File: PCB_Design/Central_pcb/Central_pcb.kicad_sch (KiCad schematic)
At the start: 1 part, among them U3 nRF52832-QFxx

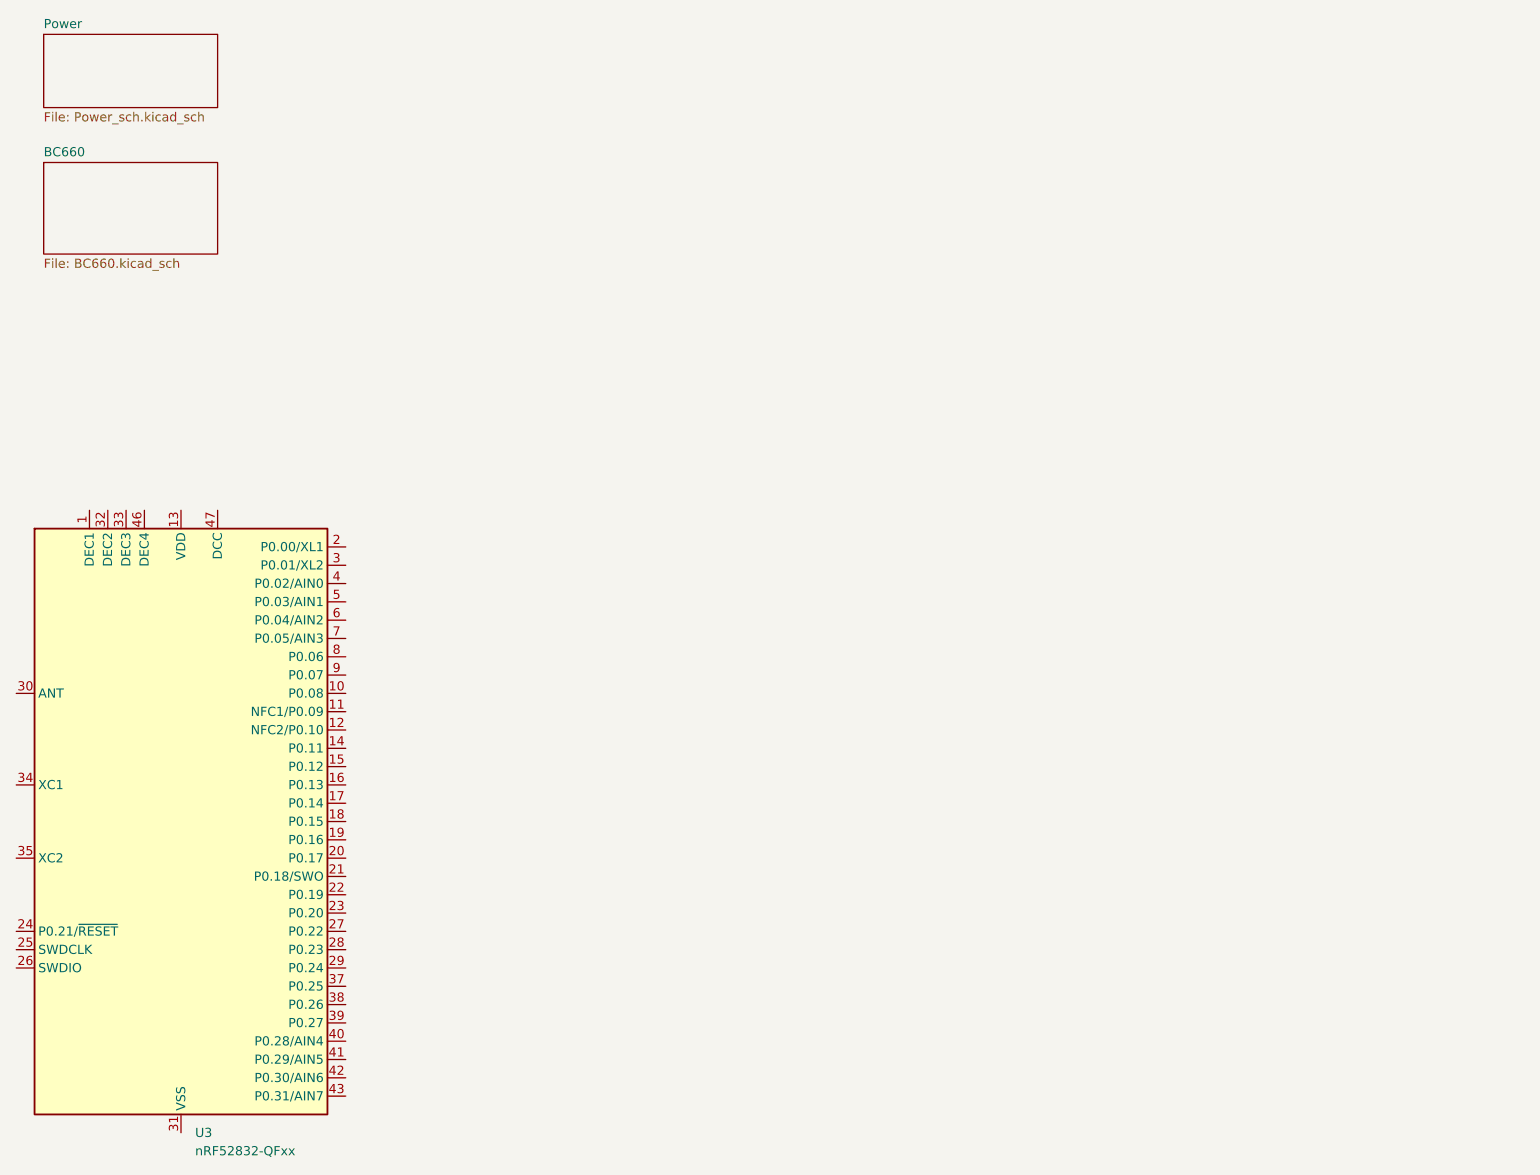
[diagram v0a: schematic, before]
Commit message: Power part added
Power part is finished with power footprints
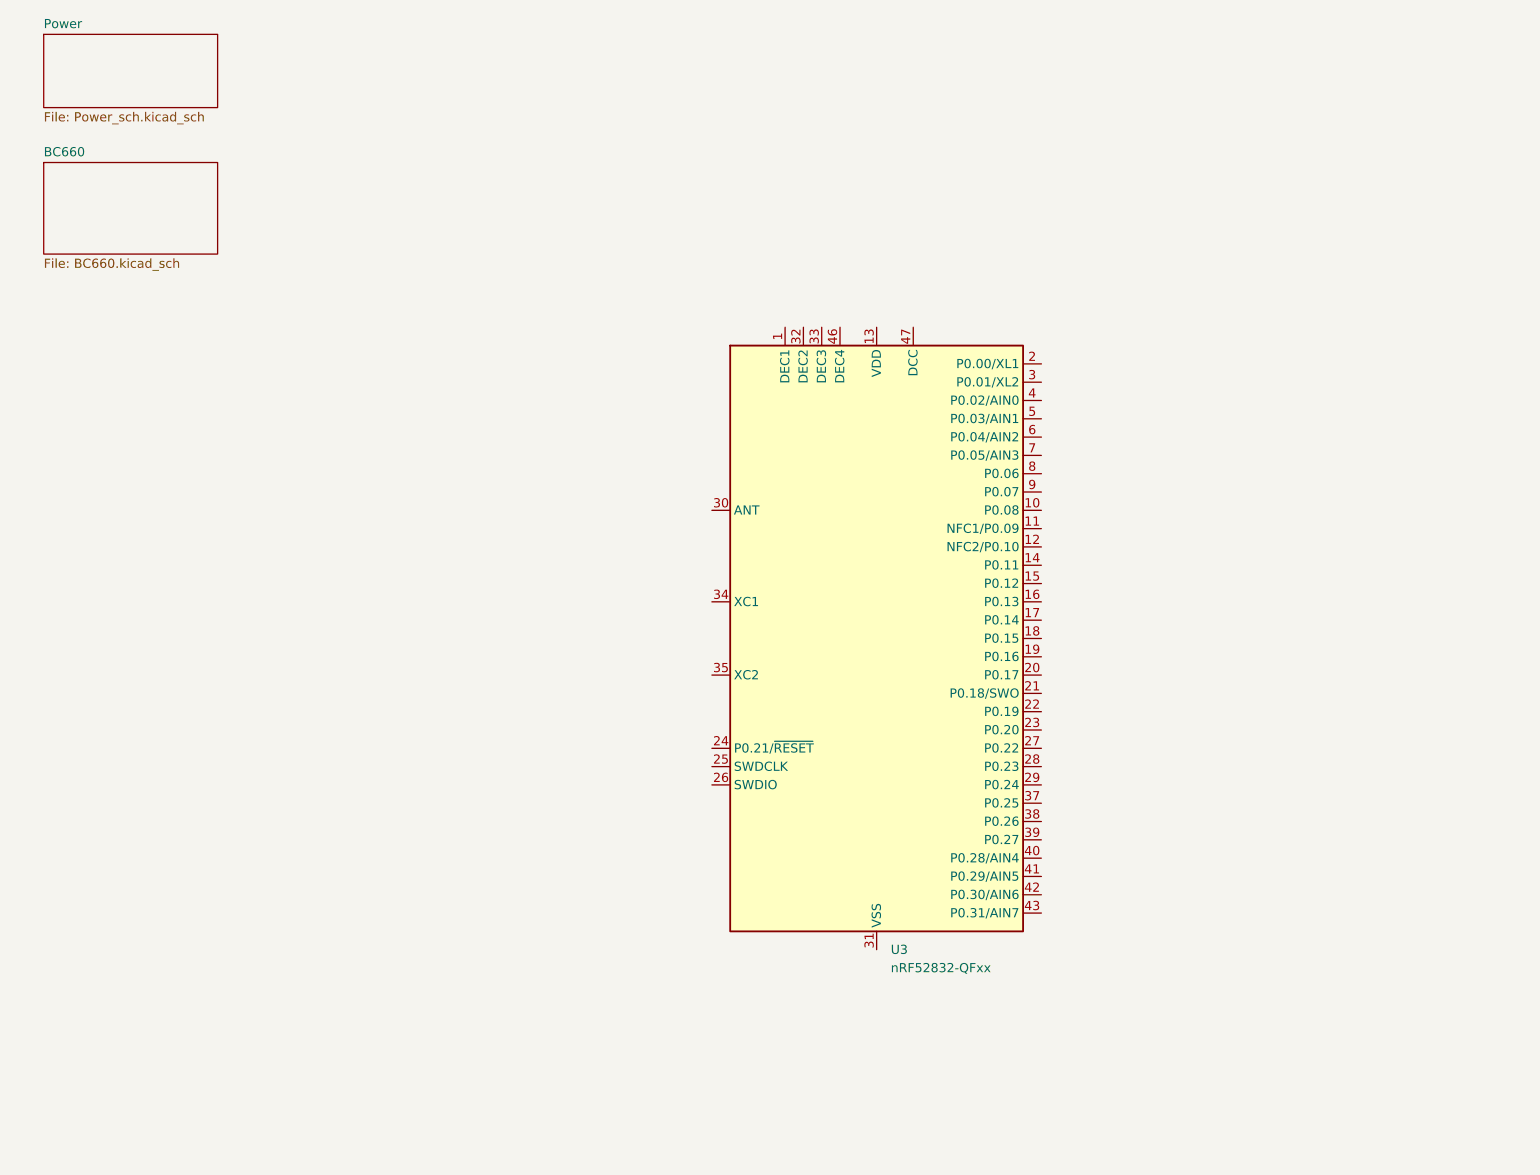
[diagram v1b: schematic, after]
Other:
- moved on the sheet: U3
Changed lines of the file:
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@@
 (kicad_sch (version 20230121) (generator eeschema)
   (paper "A4")
-  (symbol (lib_id "MCU_Nordic:nRF52832-QFxx") (at 45.72 132.08 0) (unit 1)
+  (symbol (lib_id "MCU_Nordic:nRF52832-QFxx") (at 142.24 106.68 0) (unit 1)
     (in_bom yes) (on_board yes) (dnp no) (fields_autoplaced)
-    (property "Reference" "U3" (at 47.6759 175.26 0)
+    (property "Reference" "U3" (at 144.1959 149.86 0)
       (effects (font (size 1.27 1.27)) (justify left))
     )
-    (property "Value" "nRF52832-QFxx" (at 47.6759 177.8 0)
+    (property "Value" "nRF52832-QFxx" (at 144.1959 152.4 0)
       (effects (font (size 1.27 1.27)) (justify left))
     )
-    (property "Footprint" "Package_DFN_QFN:QFN-48-1EP_6x6mm_P0.4mm_EP4.6x4.6mm" (at 45.72 185.42 0)
+    (property "Footprint" "Package_DFN_QFN:QFN-48-1EP_6x6mm_P0.4mm_EP4.6x4.6mm" (at 142.24 160.02 0)
       (effects (font (size 1.27 1.27)) hide)
     )
-    (property "Datasheet" "http://infocenter.nordicsemi.com/pdf/nRF52832_PS_v1.4.pdf" (at 33.02 127 0)
+    (property "Datasheet" "http://infocenter.nordicsemi.com/pdf/nRF52832_PS_v1.4.pdf" (at 129.54 101.6 0)
       (effects (font (size 1.27 1.27)) hide)
     )

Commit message: nrf52832 datasheet setup
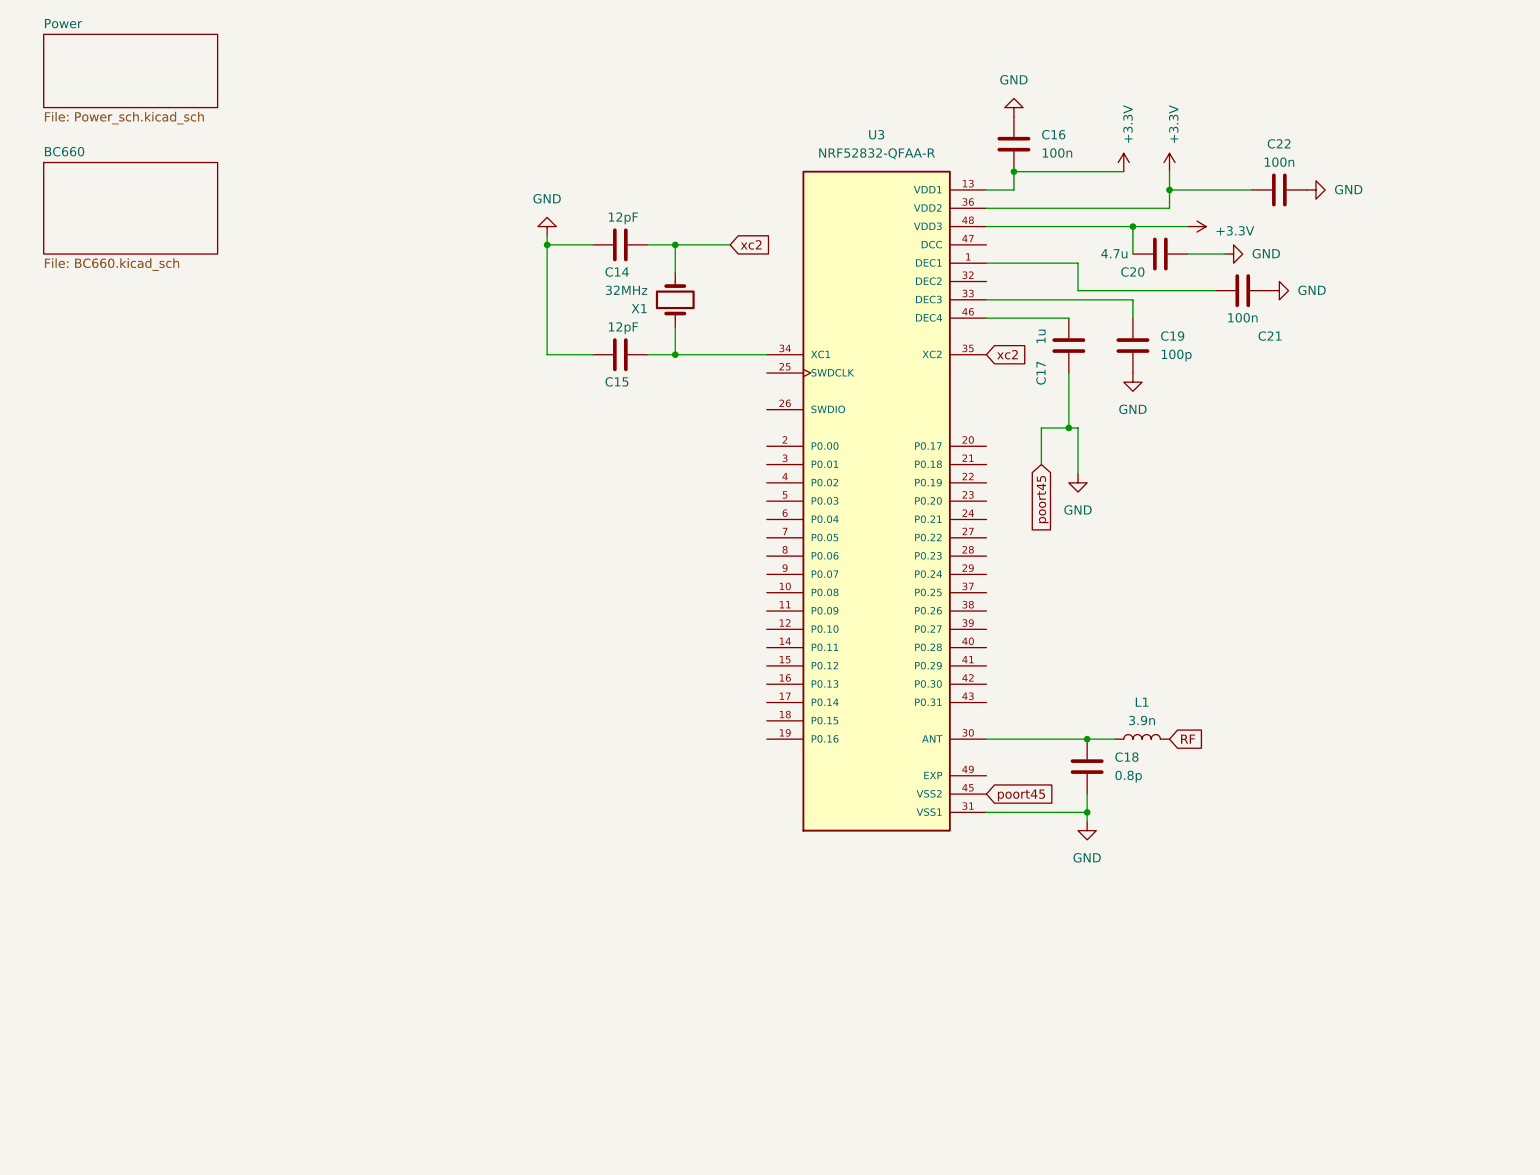
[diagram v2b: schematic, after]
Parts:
- removed U3: nRF52832-QFxx, Package_DFN_QFN:QFN-48-1EP_6x6mm_P0.4mm_EP4.6x4.6mm, symbol MCU_Nordic:nRF52832-QFxx
- added C14, C15: 12pF, symbol Device:C
- added C16, C21, C22: 100n, symbol Device:C
- added C17: 1u, symbol Device:C
- added C18: 0.8p, symbol Device:C
- added C19: 100p, symbol Device:C
- added C20: 4.7u, symbol Device:C
- added L1: 3.9n, symbol Device:L
- added U3: NRF52832-QFAA-R, NRF52832-QFAA-R:QFN40P600X600X90-49N, symbol NRF52832-QFAA-R:NRF52832-QFAA-R
- added X1: 32MHz, symbol Device:Crystal
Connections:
- new net: C19.1, U3.33 (DEC3)
- new net: C21.1, U3.1 (DEC1)
- new net: C18.2, L1.1, U3.30 (ANT)
- new net: C15.2, U3.34 (XC1), X1.1
- new net: C17.1, U3.46 (DEC4)
- new net +3.3V: C16.1, C20.2, C22.1, U3.13 (VDD1), U3.36 (VDD2), U3.48 (VDD3)
- new net GND: C14.1, C15.1, C16.2, C17.2, C18.1, C19.2, C20.1, C21.2, C22.2, U3.31 (VSS1), U3.45 (VSS2)
- new net RF: L1.2
- new net xc2: C14.2, U3.35 (XC2), X1.2

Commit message: Scematic update
update scematic and added some footrpints
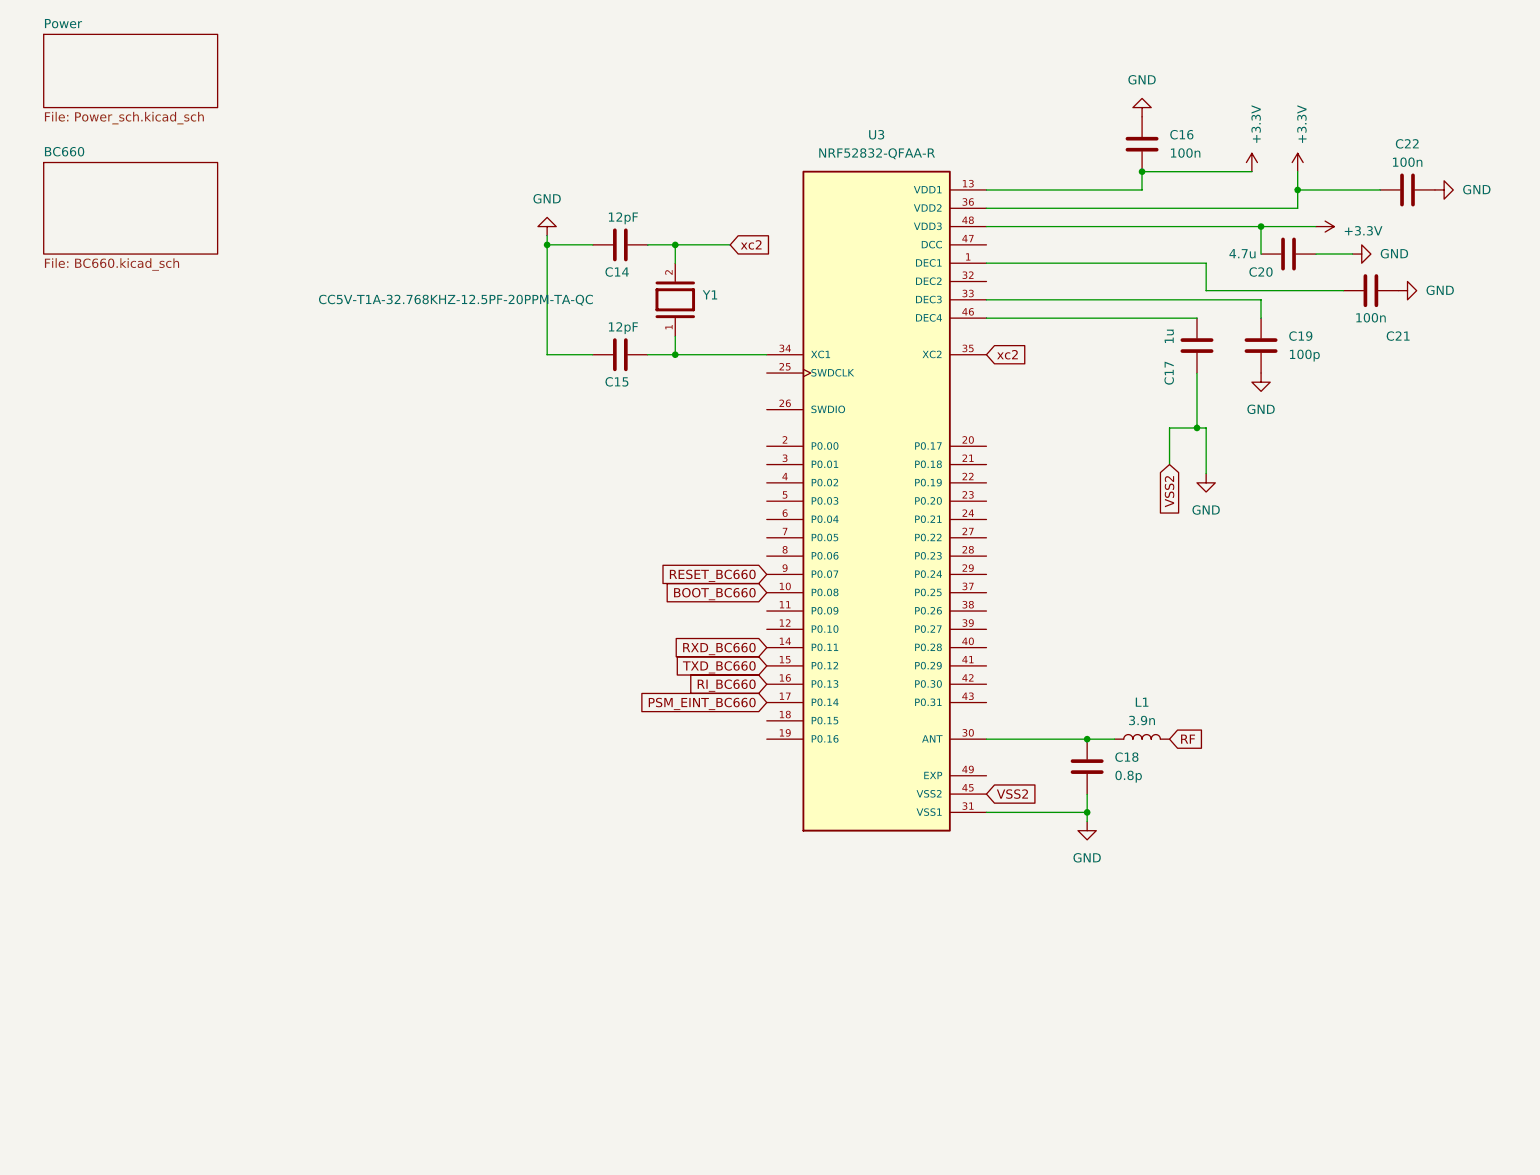
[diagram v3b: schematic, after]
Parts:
- removed X1: 32MHz, symbol Device:Crystal
- added Y1: CC5V-T1A-32.768KHZ-12.5PF-20PPM-TA-QC, Central:XTAL_CC5V-T1A-32.768KHZ-12.5PF-20PPM-TA-QC, symbol CRISTAL:CC5V-T1A-32.768KHZ-12.5PF-20PPM-TA-QC
- U3: footprint NRF52832-QFAA-R:QFN40P600X600X90-49N -> Central:QFN40P600X600X90-49N
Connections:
- net xc2: now also Y1.2
- net BOOT_BC660: now reaches U3.10 (P0.08)
- net RXD_BC660: now reaches U3.14 (P0.11)
- net TXD_BC660: now reaches U3.15 (P0.12)
- net RI_BC660: now reaches U3.16 (P0.13)
- net PSM_EINT_BC660: now reaches U3.17 (P0.14)
- net at C15.2, U3.34 (XC1): now also Y1.1
- net RESET_BC660: now reaches U3.9 (P0.07)
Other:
- moved on the sheet: C16, C17, C19, C20, C21, C22

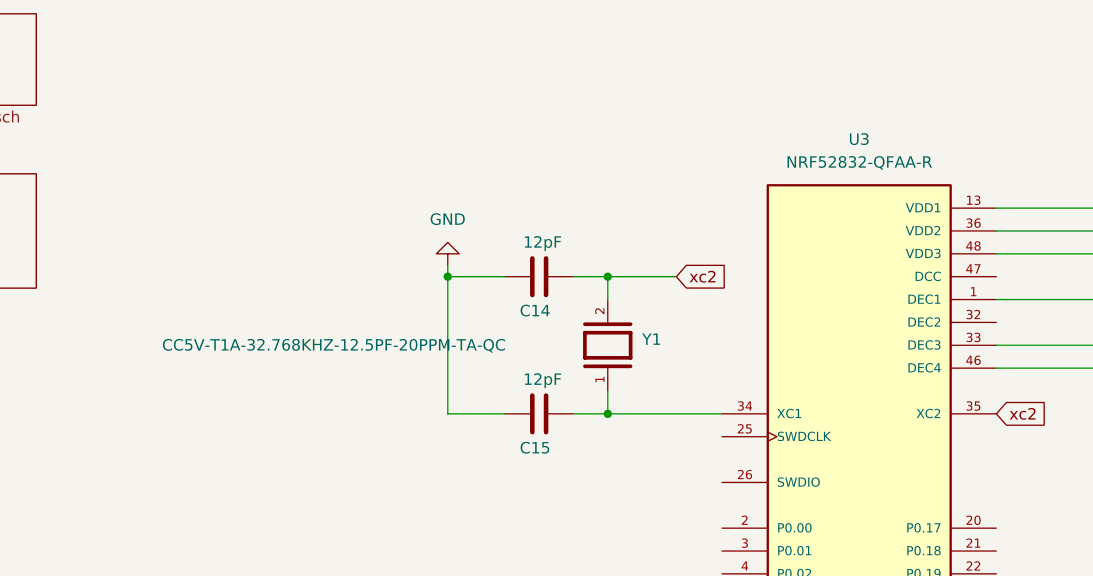
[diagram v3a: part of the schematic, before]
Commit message: Change of crystal
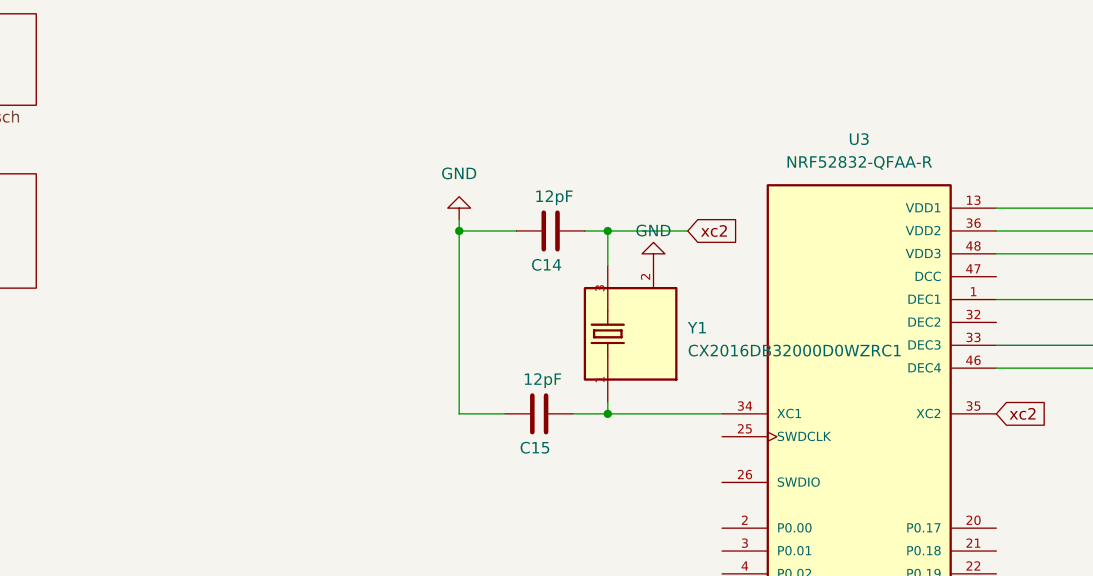
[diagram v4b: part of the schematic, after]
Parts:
- removed Y1: CC5V-T1A-32.768KHZ-12.5PF-20PPM-TA-QC, Central:XTAL_CC5V-T1A-32.768KHZ-12.5PF-20PPM-TA-QC, symbol CRISTAL:CC5V-T1A-32.768KHZ-12.5PF-20PPM-TA-QC
- added Y1: CX2016DB32000D0WZRC1, CX2016DB32000D0WZRC1:OSCCC200X160X45N, symbol 32Mhz crystal:CX2016DB32000D0WZRC1
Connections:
- net GND: now also Y1.2
- net xc2: now also Y1.3
- net at C15.2, U3.34 (XC1): now also Y1.1
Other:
- moved on the sheet: C14
